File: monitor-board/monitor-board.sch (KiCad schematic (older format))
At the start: 2 parts

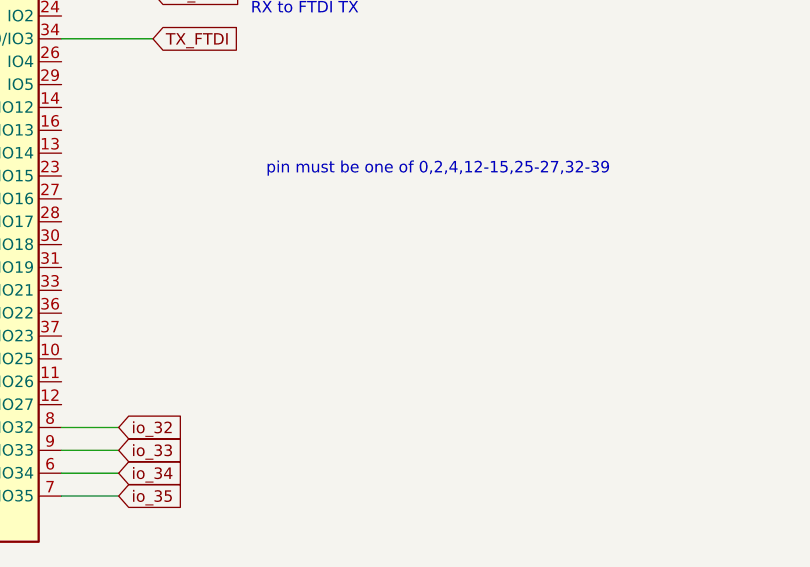
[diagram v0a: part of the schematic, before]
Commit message: note down parts that I'm using
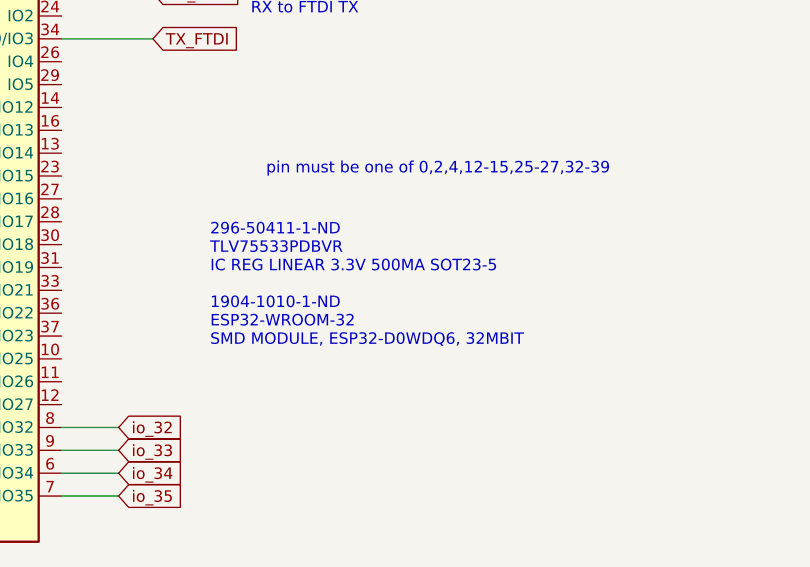
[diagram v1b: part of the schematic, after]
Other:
- note added: "296-50411-1-ND‎\n‎TLV75533PDBVR‎\nIC REG LINEAR 3.3V 500MA SOT23-5 \n\n1904-1010-1-ND‎\n‎ESP32-WROOM-32‎\nSMD MODULE, ESP32-D0WDQ6, 32MBIT"
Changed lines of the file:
@@
 EESchema Schematic File Version 4
+LIBS:monitor-board-cache
 EELAYER 30 0
 EELAYER END
@@
 Wire Wire Line
 	3000 4100 3250 4100
+Text Notes 3650 3450 0    50   ~ 0
+296-50411-1-ND‎\n‎TLV75533PDBVR‎\nIC REG LINEAR 3.3V 500MA SOT23-5 \n\n1904-1010-1-ND‎\n‎ESP32-WROOM-32‎\nSMD MODULE, ESP32-D0WDQ6, 32MBIT
 $EndSCHEMATC

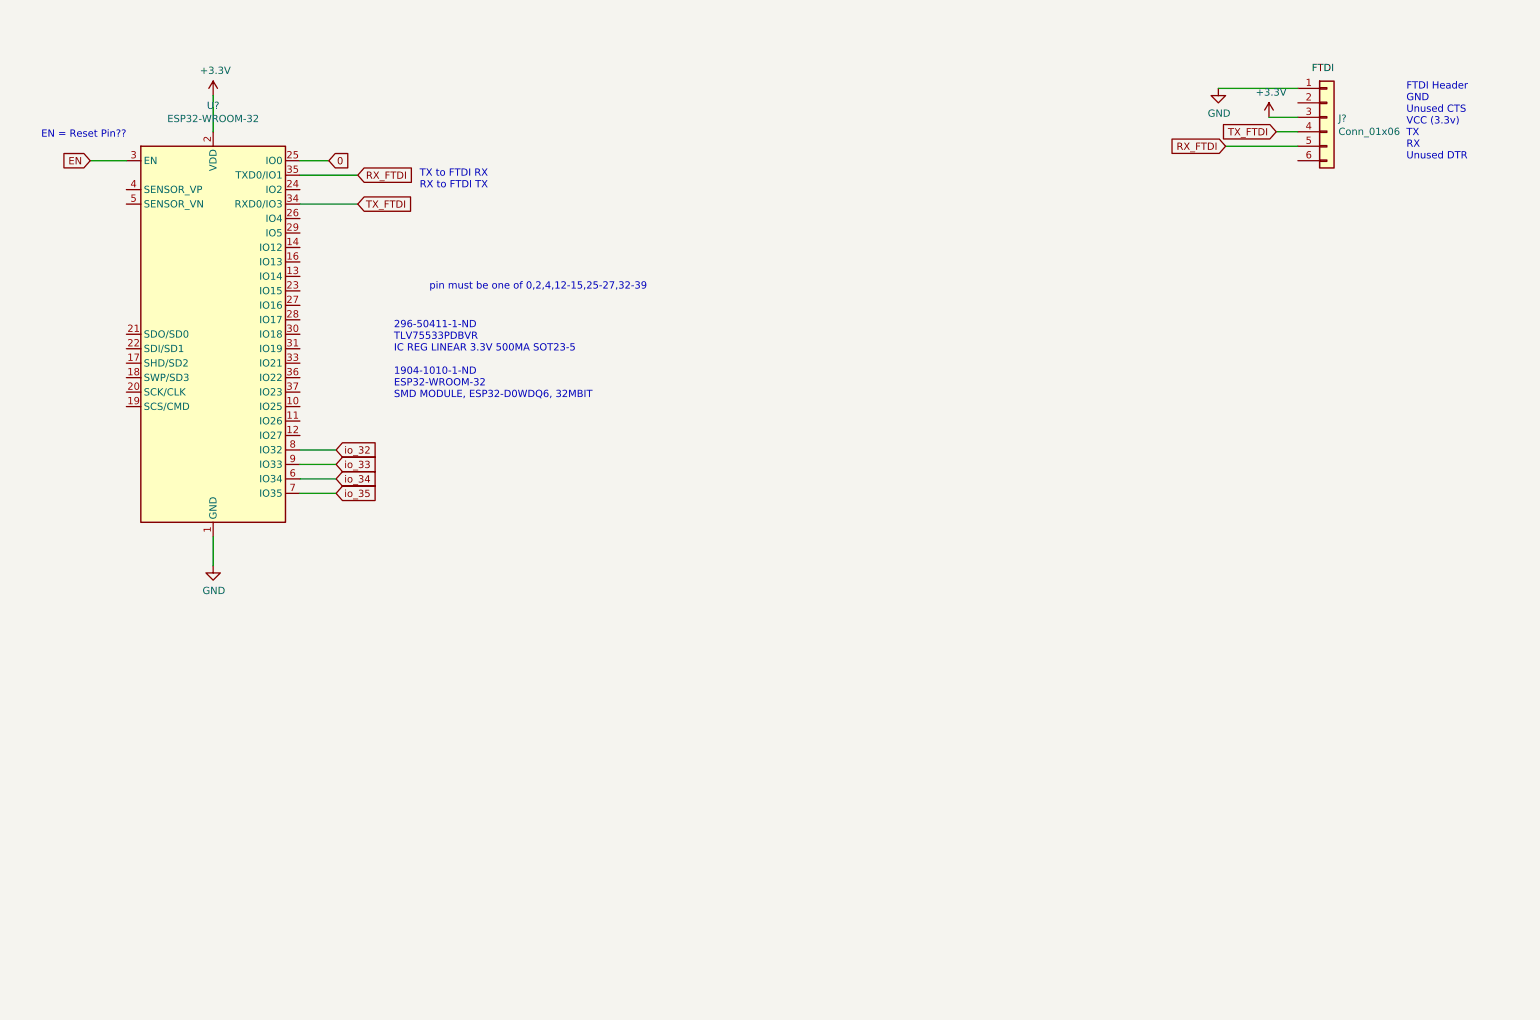
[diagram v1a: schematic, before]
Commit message: finish first version of monitor board schematic
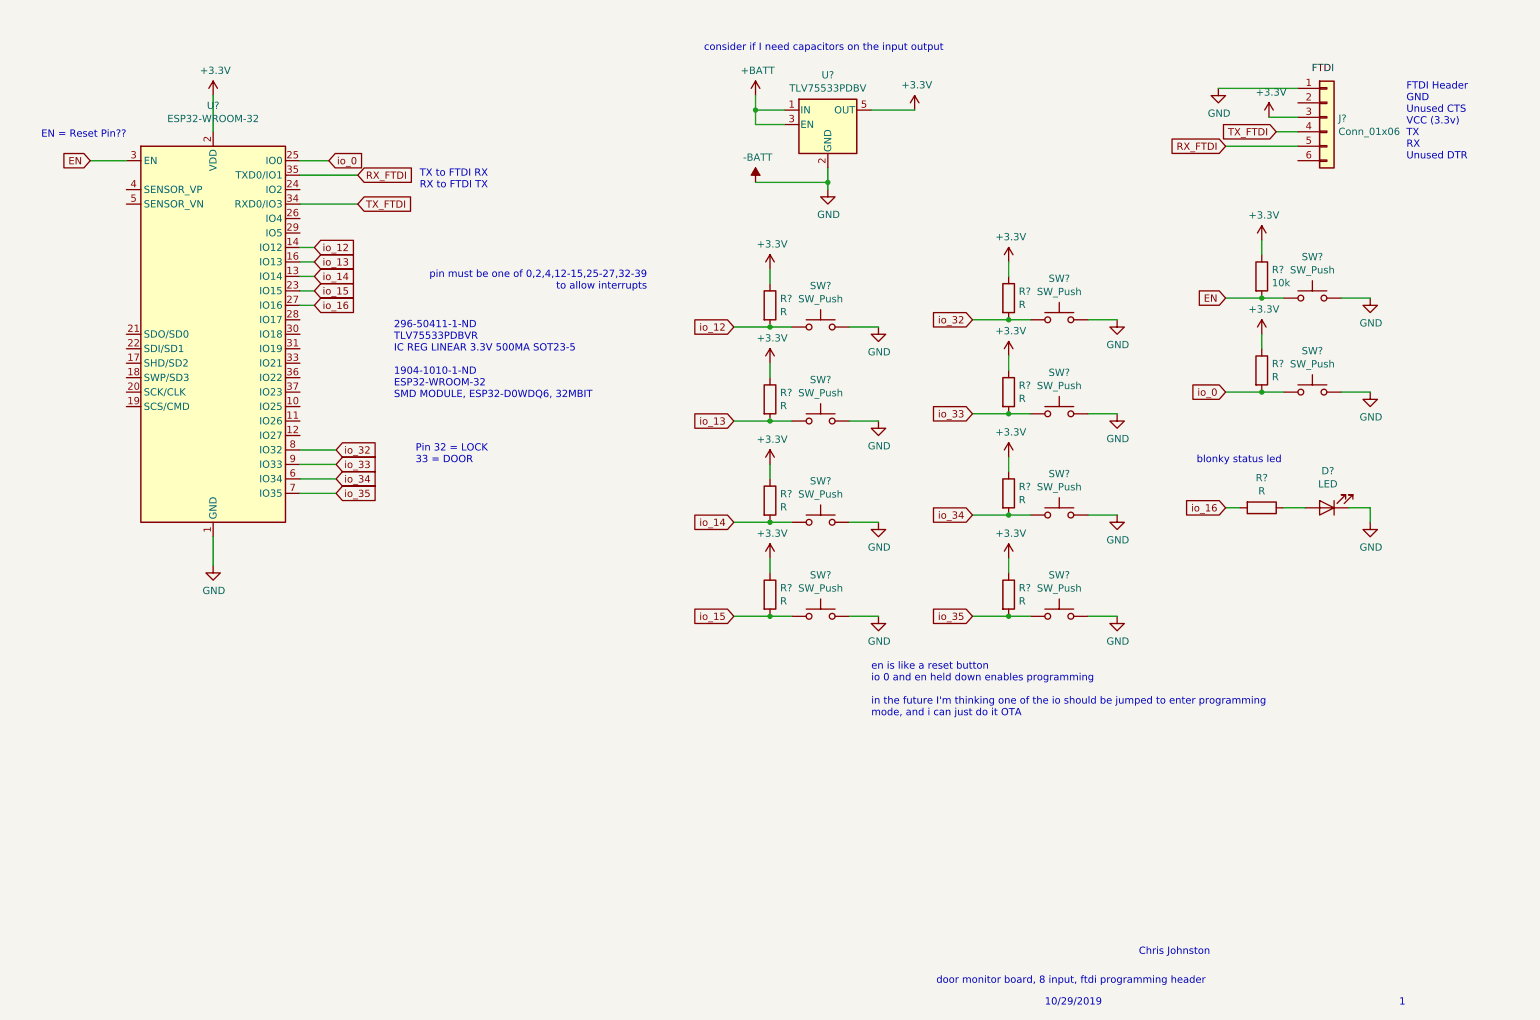
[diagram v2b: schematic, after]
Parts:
- added D?: LED, symbol Device:LED
- added R? (x10): R, symbol Device:R
- added R?: 10k, symbol Device:R
- added SW? (x10): SW_Push, symbol Switch:SW_Push
- added U?: TLV75533PDBV, Package_TO_SOT_SMD:SOT-23-5, symbol Regulator_Linear:TLV75533PDBV
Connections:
- net +3V3: now also R?.1, R?.1, R?.1, R?.1, R?.1, R?.1, R?.1, R?.1, R?.1, R?.1, U?.5 (OUT)
- net EN: now also R?.2, SW?.1
- net io_32: now also R?.2, SW?.1
- net io_33: now also R?.2, SW?.1
- net io_34: now also R?.2, SW?.1
- net io_35: now also R?.2, SW?.1
- net io_14: now reaches U?.13 (IO14)
- net io_14: now also R?.2, SW?.1
- net io_12: now reaches U?.14 (IO12)
- net io_12: now also R?.2, SW?.1
- net io_13: now reaches U?.16 (IO13)
- net io_13: now also R?.2, SW?.1
- net io_15: now reaches U?.23 (IO15)
- net io_15: now also R?.2, SW?.1
- net io_16: now reaches U?.27 (IO16)
- net io_16: now also R?.2
- net 0 renamed io_0
- net io_0: now also R?.2, SW?.1
- net GND renamed -BATT
- net -BATT: now also D?.1 (K), SW?.2, SW?.2, SW?.2, SW?.2, SW?.2, SW?.2, SW?.2, SW?.2, SW?.2, SW?.2, U?.2 (GND)
- new net: D?.2 (A), R?.1
- new net +BATT: U?.1 (IN), U?.3 (EN)
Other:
- note added: "1"
- note added: "10/29/2019"
- note added: "Chris Johnston"
- note added: "Pin 32 = LOCK\n33 = DOOR"
- note added: "blonky status led"
- note added: "consider if I need capacitors on the input output"
- note added: "door monitor board, 8 input, ftdi programming header"
- note added: "en is like a reset button\nio 0 and en held down enables programming\n\nin the future I'm thinking one of the io should be jumped to enter programming\nmode, and i can just do it OTA"
- note added: "pin must be one of 0,2,4,12-15,25-27,32-39\nto allow interrupts"
- note removed: "pin must be one of 0,2,4,12-15,25-27,32-39"

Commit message: setup footprints
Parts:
- added JBAT1: Conn_01x02, TerminalBlock_Phoenix:TerminalBlock_Phoenix_PT-1,5-2-5.0-H_1x02_P5.00mm_Horizontal, symbol Connector_Generic:Conn_01x02
- D1: renamed from D?; footprint (none) -> LED_SMD:LED_2816_7142Metric_Pad3.20x4.45mm_HandSolder
- J1: renamed from J?; footprint (none) -> Connector_PinSocket_2.54mm:PinSocket_1x06_P2.54mm_Vertical
- R1, R10, R2, R3, R4, R5, R6, R7, R8: renamed from R?; value R -> 10k; footprint (none) -> Resistor_SMD:R_0805_2012Metric_Pad1.15x1.40mm_HandSolder
- R11: renamed from R?; value R -> 330; footprint (none) -> Resistor_SMD:R_0805_2012Metric_Pad1.15x1.40mm_HandSolder
- R9: renamed from R?; footprint (none) -> Resistor_SMD:R_0805_2012Metric_Pad1.15x1.40mm_HandSolder
- SW1, SW10, SW2, SW3, SW4, SW5, SW6, SW7, SW8, SW9: renamed from SW?; footprint (none) -> TerminalBlock_Phoenix:TerminalBlock_Phoenix_PT-1,5-2-5.0-H_1x02_P5.00mm_Horizontal
- gave numbers to parts that had none: 2
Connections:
- net +3V3: no longer J1.3 (Pin_3)
- net +BATT: now also JBAT1.1 (Pin_1)
- net -BATT: now also JBAT1.2 (Pin_2)
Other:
- note added: "16 = LED"
- note added: "FTDI Header\nGND\nUnused CTS\nUnused VCC (3.3v)\nTX\nRX\nUnused DTR"
- note added: "FTDI header cannot power esp32 for programming\nInstead, bridge together the grounds\nand supply power with battery through regulator when\nprogramming"
- note added: "ensure tx and rx are 3.3v"
- note added: "range is up to 5.5v"
- note removed: "FTDI Header\nGND\nUnused CTS\nVCC (3.3v)\nTX\nRX\nUnused DTR"

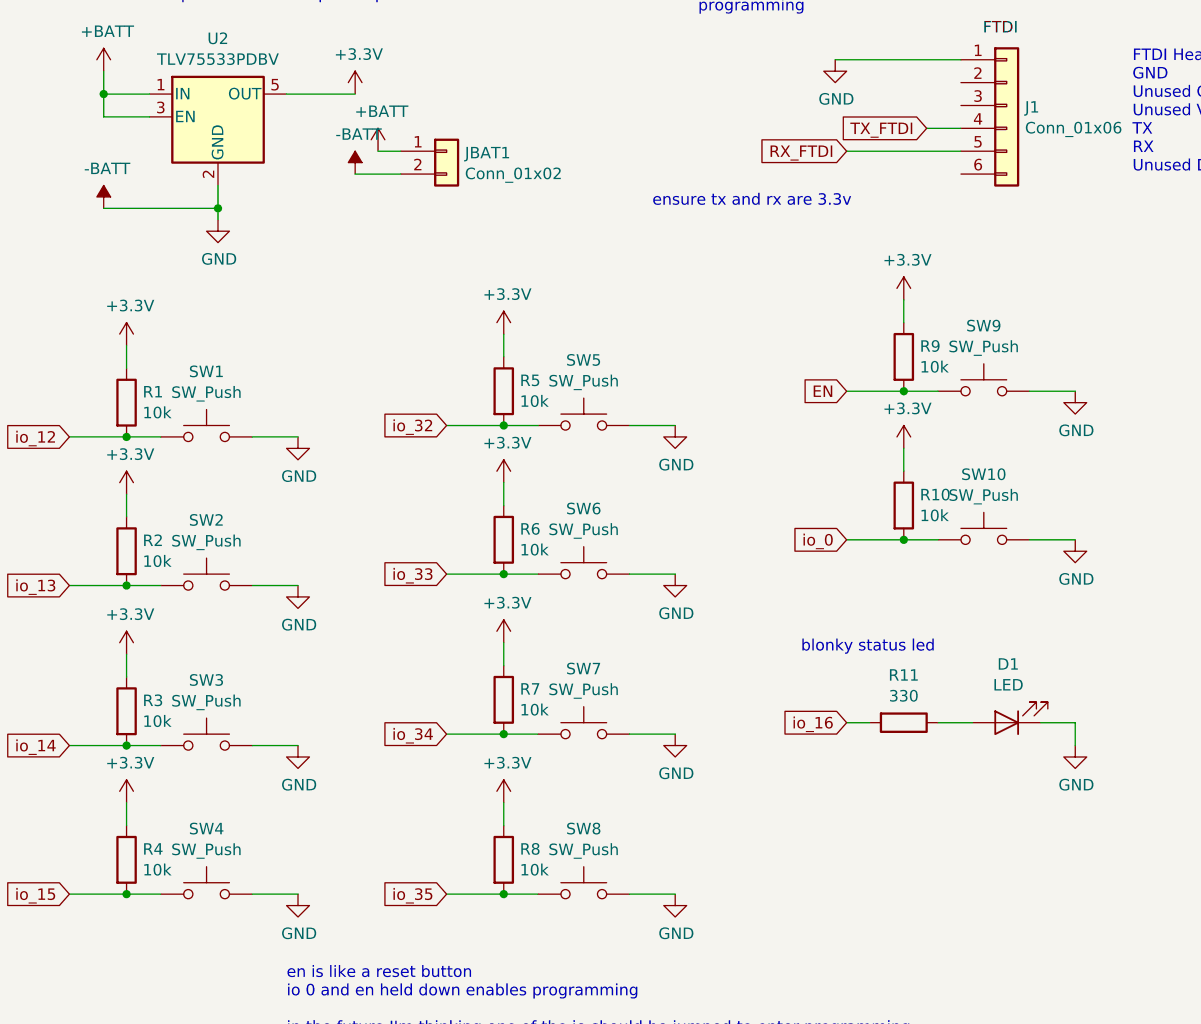
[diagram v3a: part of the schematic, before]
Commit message: initial layout of footprints
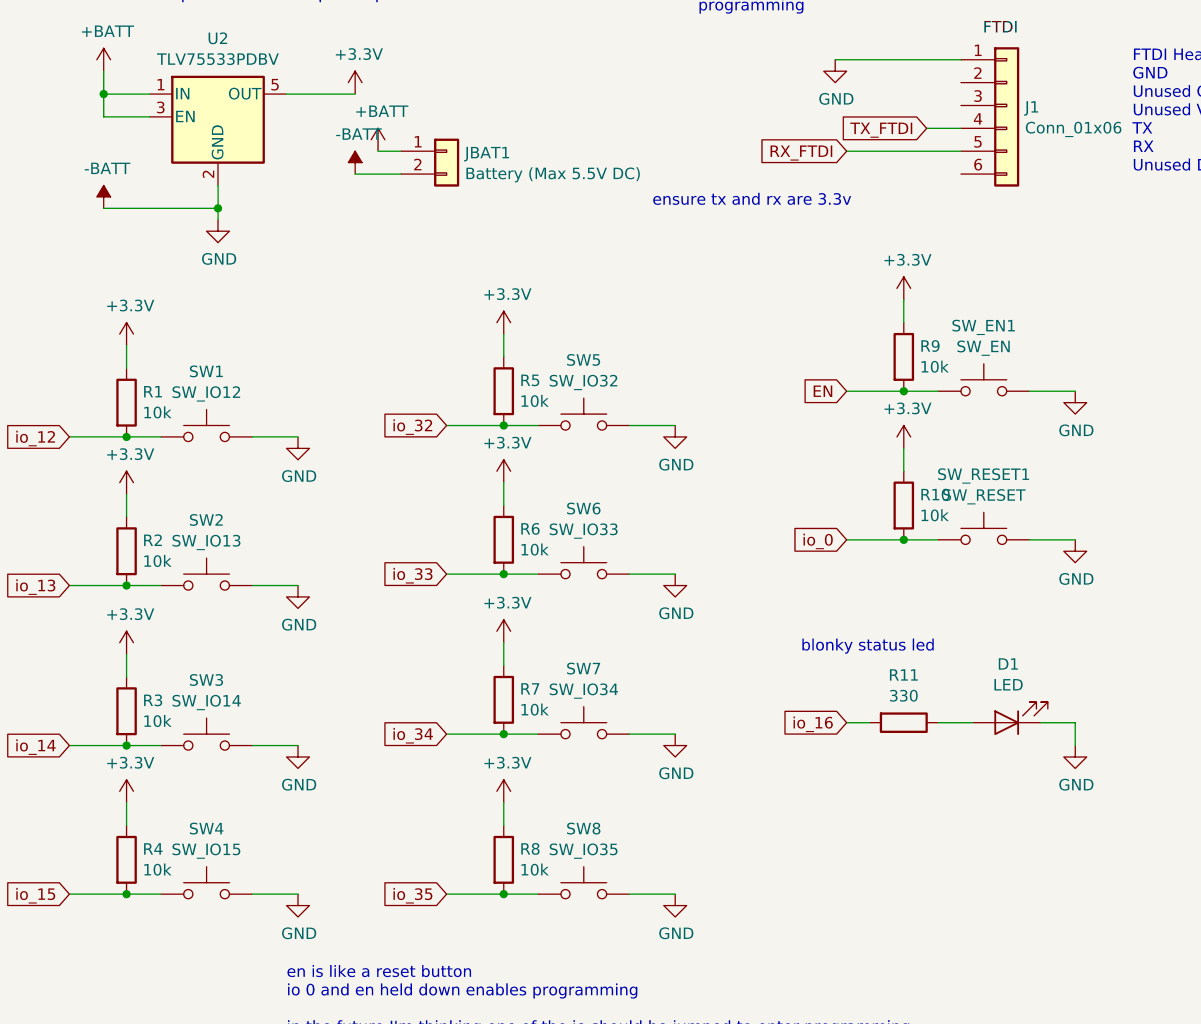
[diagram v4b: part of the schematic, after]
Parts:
- JBAT1: value Conn_01x02 -> Battery (Max 5.5V DC)
- SW1: value SW_Push -> SW_IO12
- SW2: value SW_Push -> SW_IO13
- SW3: value SW_Push -> SW_IO14
- SW4: value SW_Push -> SW_IO15
- SW5: value SW_Push -> SW_IO32
- SW6: value SW_Push -> SW_IO33
- SW7: value SW_Push -> SW_IO34
- SW8: value SW_Push -> SW_IO35
- SW_EN1: renamed from SW9; value SW_Push -> SW_EN
- SW_RESET1: renamed from SW10; value SW_Push -> SW_RESET
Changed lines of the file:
@@
 P 6600 2950
 F 0 "SW1" H 6600 3235 50  0000 C CNN
-F 1 "SW_Push" H 6600 3144 50  0000 C CNN
+F 1 "SW_IO12" H 6600 3144 50  0000 C CNN
 F 2 "TerminalBlock_Phoenix:TerminalBlock_Phoenix_PT-1,5-2-5.0-H_1x02_P5.00mm_Horizontal" H 6600 3150 50  0001 C CNN
 F 3 "~" H 6600 3150 50  0001 C CNN
@@
 P 6600 3600
 F 0 "SW2" H 6600 3885 50  0000 C CNN
-F 1 "SW_Push" H 6600 3794 50  0000 C CNN
+F 1 "SW_IO13" H 6600 3794 50  0000 C CNN
 F 2 "TerminalBlock_Phoenix:TerminalBlock_Phoenix_PT-1,5-2-5.0-H_1x02_P5.00mm_Horizontal" H 6600 3800 50  0001 C CNN
 F 3 "~" H 6600 3800 50  0001 C CNN
@@
 P 6600 4300
 F 0 "SW3" H 6600 4585 50  0000 C CNN
-F 1 "SW_Push" H 6600 4494 50  0000 C CNN
+F 1 "SW_IO14" H 6600 4494 50  0000 C CNN
 F 2 "TerminalBlock_Phoenix:TerminalBlock_Phoenix_PT-1,5-2-5.0-H_1x02_P5.00mm_Horizontal" H 6600 4500 50  0001 C CNN
 F 3 "~" H 6600 4500 50  0001 C CNN
@@
 P 6600 4950
 F 0 "SW4" H 6600 5235 50  0000 C CNN
-F 1 "SW_Push" H 6600 5144 50  0000 C CNN
+F 1 "SW_IO15" H 6600 5144 50  0000 C CNN
 F 2 "TerminalBlock_Phoenix:TerminalBlock_Phoenix_PT-1,5-2-5.0-H_1x02_P5.00mm_Horizontal" H 6600 5150 50  0001 C CNN
 F 3 "~" H 6600 5150 50  0001 C CNN
@@
 P 8250 2900
 F 0 "SW5" H 8250 3185 50  0000 C CNN
-F 1 "SW_Push" H 8250 3094 50  0000 C CNN
+F 1 "SW_IO32" H 8250 3094 50  0000 C CNN
 F 2 "TerminalBlock_Phoenix:TerminalBlock_Phoenix_PT-1,5-2-5.0-H_1x02_P5.00mm_Horizontal" H 8250 3100 50  0001 C CNN
 F 3 "~" H 8250 3100 50  0001 C CNN
@@
 P 8250 3550
 F 0 "SW6" H 8250 3835 50  0000 C CNN
-F 1 "SW_Push" H 8250 3744 50  0000 C CNN
+F 1 "SW_IO33" H 8250 3744 50  0000 C CNN
 F 2 "TerminalBlock_Phoenix:TerminalBlock_Phoenix_PT-1,5-2-5.0-H_1x02_P5.00mm_Horizontal" H 8250 3750 50  0001 C CNN
 F 3 "~" H 8250 3750 50  0001 C CNN
@@
 P 8250 4250
 F 0 "SW7" H 8250 4535 50  0000 C CNN
-F 1 "SW_Push" H 8250 4444 50  0000 C CNN
+F 1 "SW_IO34" H 8250 4444 50  0000 C CNN
 F 2 "TerminalBlock_Phoenix:TerminalBlock_Phoenix_PT-1,5-2-5.0-H_1x02_P5.00mm_Horizontal" H 8250 4450 50  0001 C CNN
 F 3 "~" H 8250 4450 50  0001 C CNN
@@
 P 8250 4950
 F 0 "SW8" H 8250 5235 50  0000 C CNN
-F 1 "SW_Push" H 8250 5144 50  0000 C CNN
+F 1 "SW_IO35" H 8250 5144 50  0000 C CNN
 F 2 "TerminalBlock_Phoenix:TerminalBlock_Phoenix_PT-1,5-2-5.0-H_1x02_P5.00mm_Horizontal" H 8250 5150 50  0001 C CNN
 F 3 "~" H 8250 5150 50  0001 C CNN
@@
 	9650 2450 9650 2350
 $Comp
-L Switch:SW_Push SW9
+L Switch:SW_Push SW_EN1
 U 1 1 5DBC4F66
 P 10000 2750
-F 0 "SW9" H 10000 3035 50  0000 C CNN
-F 1 "SW_Push" H 10000 2944 50  0000 C CNN
+F 0 "SW_EN1" H 10000 3035 50  0000 C CNN
+F 1 "SW_EN" H 10000 2944 50  0000 C CNN
 F 2 "TerminalBlock_Phoenix:TerminalBlock_Phoenix_PT-1,5-2-5.0-H_1x02_P5.00mm_Horizontal" H 10000 2950 50  0001 C CNN
 F 3 "~" H 10000 2950 50  0001 C CNN
@@
 	9650 3100 9650 3000
 $Comp
-L Switch:SW_Push SW10
+L Switch:SW_Push SW_RESET1
 U 1 1 5DBD04BF
 P 10000 3400
-F 0 "SW10" H 10000 3685 50  0000 C CNN
-F 1 "SW_Push" H 10000 3594 50  0000 C CNN
+F 0 "SW_RESET1" H 10000 3685 50  0000 C CNN
+F 1 "SW_RESET" H 10000 3594 50  0000 C CNN
 F 2 "TerminalBlock_Phoenix:TerminalBlock_Phoenix_PT-1,5-2-5.0-H_1x02_P5.00mm_Horizontal" H 10000 3600 50  0001 C CNN
 F 3 "~" H 10000 3600 50  0001 C CNN
@@
 P 7650 1700
 F 0 "JBAT1" H 7730 1692 50  0000 L CNN
-F 1 "Conn_01x02" H 7730 1601 50  0000 L CNN
+F 1 "Battery (Max 5.5V DC)" H 7730 1601 50  0000 L CNN
 F 2 "TerminalBlock_Phoenix:TerminalBlock_Phoenix_PT-1,5-2-5.0-H_1x02_P5.00mm_Horizontal" H 7650 1700 50  0001 C CNN
 F 3 "~" H 7650 1700 50  0001 C CNN

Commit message: fix footprints of led and switches
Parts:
- D1: footprint LED_SMD:LED_2816_7142Metric_Pad3.20x4.45mm_HandSolder -> LED_SMD:LED_0805_2012Metric_Pad1.15x1.40mm_HandSolder
- SW_EN1, SW_RESET1: footprint TerminalBlock_Phoenix:TerminalBlock_Phoenix_PT-1,5-2-5.0-H_1x02_P5.00mm_Horizontal -> Button_Switch_THT:SW_PUSH_6mm
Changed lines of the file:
@@
 F 0 "SW_EN1" H 10000 3035 50  0000 C CNN
 F 1 "SW_EN" H 10000 2944 50  0000 C CNN
-F 2 "TerminalBlock_Phoenix:TerminalBlock_Phoenix_PT-1,5-2-5.0-H_1x02_P5.00mm_Horizontal" H 10000 2950 50  0001 C CNN
+F 2 "Button_Switch_THT:SW_PUSH_6mm" H 10000 2950 50  0001 C CNN
 F 3 "~" H 10000 2950 50  0001 C CNN
 	1    10000 2750
@@
 F 0 "SW_RESET1" H 10000 3685 50  0000 C CNN
 F 1 "SW_RESET" H 10000 3594 50  0000 C CNN
-F 2 "TerminalBlock_Phoenix:TerminalBlock_Phoenix_PT-1,5-2-5.0-H_1x02_P5.00mm_Horizontal" H 10000 3600 50  0001 C CNN
+F 2 "Button_Switch_THT:SW_PUSH_6mm" H 10000 3600 50  0001 C CNN
 F 3 "~" H 10000 3600 50  0001 C CNN
 	1    10000 3400
@@
 F 0 "D1" H 10093 3945 50  0000 C CNN
 F 1 "LED" H 10093 4036 50  0000 C CNN
-F 2 "LED_SMD:LED_2816_7142Metric_Pad3.20x4.45mm_HandSolder" H 10100 4200 50  0001 C CNN
+F 2 "LED_SMD:LED_0805_2012Metric_Pad1.15x1.40mm_HandSolder" H 10100 4200 50  0001 C CNN
 F 3 "~" H 10100 4200 50  0001 C CNN
 	1    10100 4200
